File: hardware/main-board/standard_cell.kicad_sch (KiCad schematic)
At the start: 1 part

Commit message: stuff
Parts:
- added C1, C3, C5, C7: C, symbol Device:C
- added CH446Q1: ~, symbol SeniorDesign:CH446Q_Crossbar_Switch
- added D1, D3: 1N4148WT, Diode_SMD:D_SOD-523, symbol Diode:1N4148WT
- added Q1: PNP, symbol Simulation_SPICE:PNP
- added Q3: NPN, symbol Simulation_SPICE:NPN
- added U1: TL071, symbol Amplifier_Operational:TL071
- added U11, U3, U5, U7, U9: MCP4141-xxxx-P, Package_DIP:DIP-8_W7.62mm, symbol Potentiometer_Digital:MCP4141-xxxx-P
- renumbered CH446Q to CH446Q2
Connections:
- net Input: now also CH446Q2.33 (Y0), CH446Q1.33 (Y0)
- net C1_out: now reaches CH446Q2.1 (X14)
- net C1_out: now also C1.2
- net Output: now reaches CH446Q2.11 (Y7)
- net Output: now also CH446Q1.11 (Y7)
- net GND: now reaches CH446Q2.13 (Y6)
- net GND: now also CH446Q1.13 (Y6)
- net at CH446Q2.15 (Y5): now also CH446Q1.15 (Y5)
- net at CH446Q2.17 (Y4): now also CH446Q1.17 (Y4)
- net C2_in: now reaches CH446Q2.2 (x15)
- net C2_in: now also C3.1
- net C1_in: now reaches CH446Q2.24 (X13)
- net C1_in: now also C1.1
- net R5_out: now reaches CH446Q2.25 (X12)
- net R5_out: now also U5.6 (P0W), U5.7 (P0B)
- net R2_in: now reaches CH446Q2.26 (X5)
- net R2_in: now also U7.5 (P0A)
- net R1_out: now reaches CH446Q2.27 (X4)
- net R1_out: now also U11.6 (P0W), U11.7 (P0B)
- net R1_in: now reaches CH446Q2.28 (X3)
- net R1_in: now also U11.5 (P0A)
- net Op_neg: now reaches CH446Q2.29 (X2)
- net Op_neg: now also U1.2 (-)
- net R2_out: now reaches CH446Q2.3 (X6)
- net R2_out: now also U7.6 (P0W), U7.7 (P0B)
- net Op_pos: now reaches CH446Q2.30 (X1)
- net Op_pos: now also U1.3 (+)
- net Op_out: now reaches CH446Q2.31 (X0)
- net Op_out: now also U1.6
- net at CH446Q2.35 (Y1): now also CH446Q1.35 (Y1)
- net at CH446Q2.37 (Y2): now also CH446Q1.37 (Y2)
- net at CH446Q2.39 (Y3): now also CH446Q1.39 (Y3)
- net R3_in: now reaches CH446Q2.4 (X7)
- net R3_in: now also U9.5 (P0A)
- net R3_out: now reaches CH446Q2.5 (X8)
- net R3_out: now also U9.6 (P0W), U9.7 (P0B)
- net R4_in: now reaches CH446Q2.6 (X9)
- net R4_in: now also U3.5 (P0A)
- net R4_out: now reaches CH446Q2.7 (X10)
- net R4_out: now also U3.6 (P0W), U3.7 (P0B)
- net R5_in: now reaches CH446Q2.8 (X11)
- net R5_in: now also U5.5 (P0A)
- new net +5V: U1.7 (V+), U11.8 (V_{DD}), U3.8 (V_{DD}), U5.8 (V_{DD}), U7.8 (V_{DD}), U9.8 (V_{DD})
- new net -5V: U1.4 (V-), U11.4 (V_{SS}), U3.4 (V_{SS}), U5.4 (V_{SS}), U7.4 (V_{SS}), U9.4 (V_{SS})
- new net C2_out: C3.2, CH446Q1.31 (X0)
- new net C3_in: C5.1, CH446Q1.30 (X1)
- new net C3_out: C5.2, CH446Q1.29 (X2)
- new net C4_in: C7.1, CH446Q1.28 (X3)
- new net C4_out: C7.2, CH446Q1.27 (X4)
- new net D1_anode: CH446Q1.3 (X6), D1.2 (A)
- new net D1_cathode: CH446Q1.26 (X5), D1.1 (K)
- new net D2_anode: CH446Q1.5 (X8), D3.2 (A)
- new net D2_cathode: CH446Q1.4 (X7), D3.1 (K)
- new net NPN_Emitter: Q3.3 (E)
- new net NPN_base: CH446Q1.6 (X9), Q3.2 (B)
- new net NPN_collector: CH446Q1.8 (X11), Q3.1 (C)
- new net NPN_emitter: CH446Q1.7 (X10)
- new net PNP_base: CH446Q1.25 (X12), Q1.2 (B)
- new net PNP_collector: CH446Q1.1 (X14), Q1.1 (C)
- new net PNP_emitter: CH446Q1.24 (X13), Q1.3 (E)
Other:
- note added: "Digital Potentiometers (Pins x3-12)"
- note added: "OP-AMP Block (Pins x0-2)"
- moved on the sheet: CH446Q2A

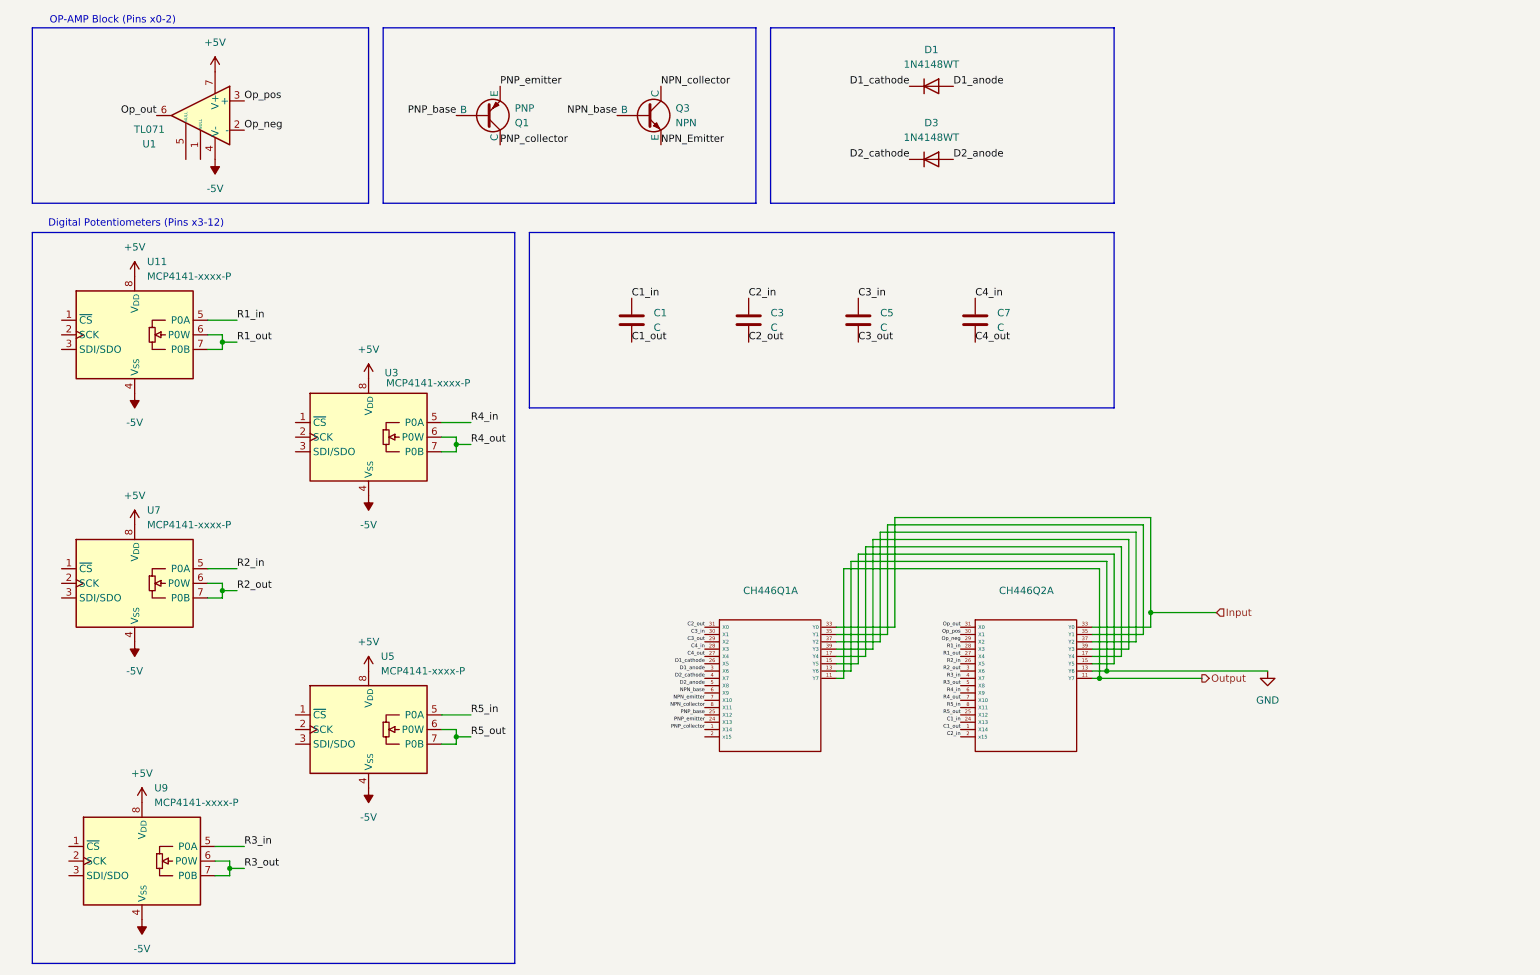
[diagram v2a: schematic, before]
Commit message: Changed cell design added new resistors
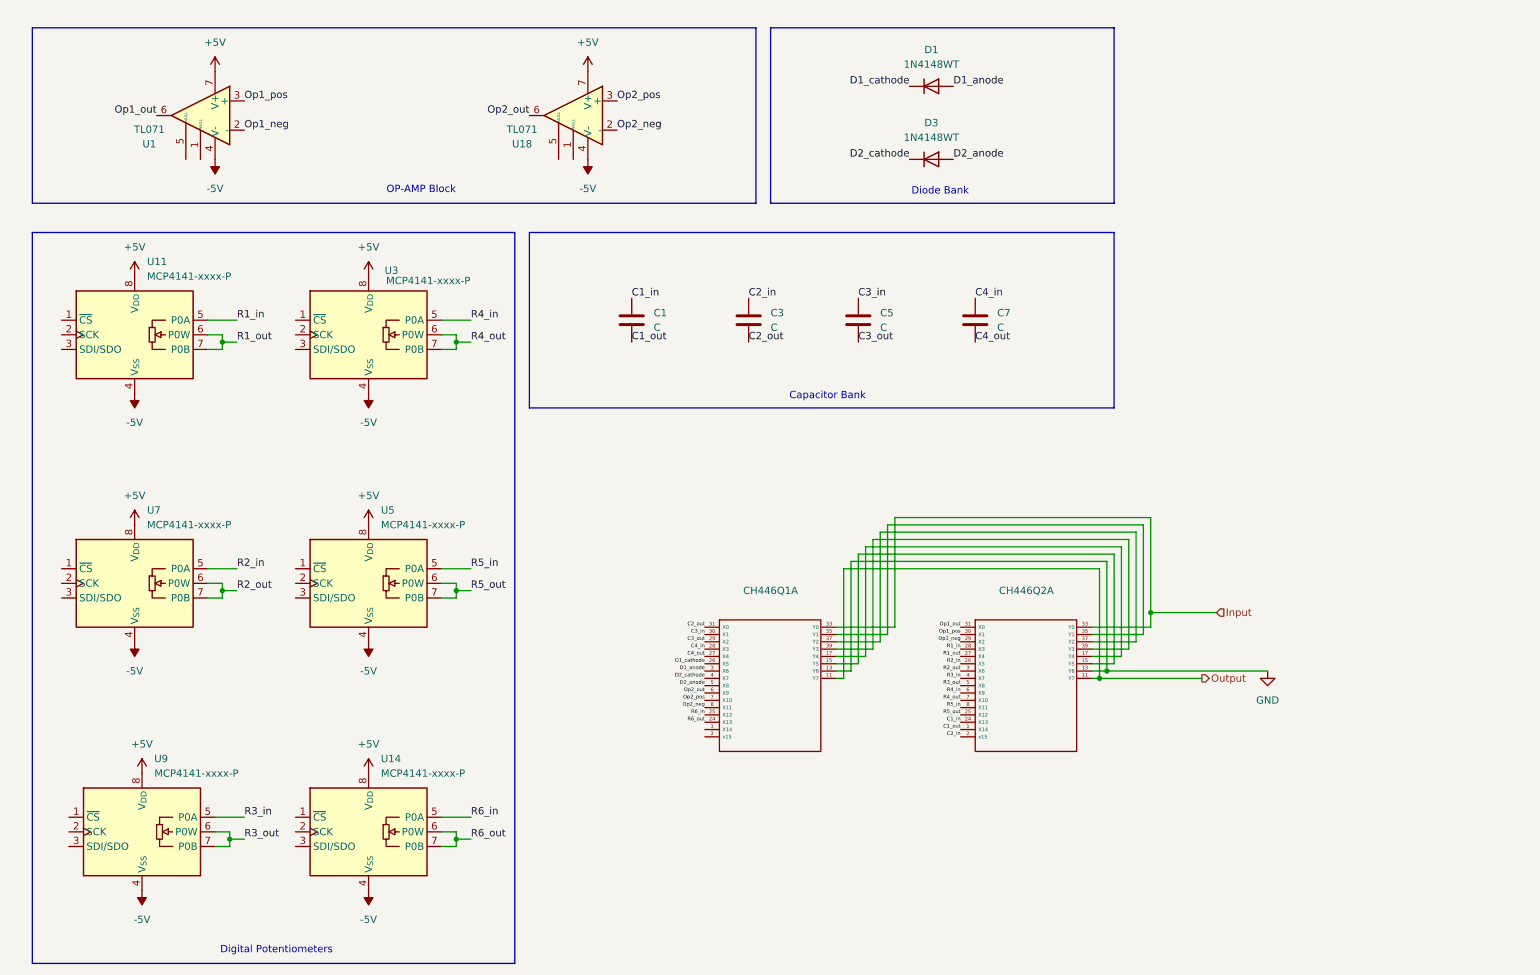
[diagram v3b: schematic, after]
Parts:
- removed Q1: PNP, symbol Simulation_SPICE:PNP
- removed Q3: NPN, symbol Simulation_SPICE:NPN
- added U14: MCP4141-xxxx-P, Package_DIP:DIP-8_W7.62mm, symbol Potentiometer_Digital:MCP4141-xxxx-P
- added U18: TL071, symbol Amplifier_Operational:TL071
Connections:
- net +5V: now also U14.8 (V_{DD}), U18.7 (V+)
- net -5V: now also U14.4 (V_{SS}), U18.4 (V-)
- net NPN_base renamed Op2_out
- net Op2_out: now also U18.6
- net NPN_collector renamed Op2_neg
- net Op2_neg: now also U18.2 (-)
- net NPN_emitter renamed Op2_pos
- net Op2_pos: now also U18.3 (+)
- net Op_neg renamed Op1_neg
- net Op_out renamed Op1_out
- net Op_pos renamed Op1_pos
- net PNP_base renamed R6_in
- net R6_in: now also U14.5 (P0A)
- net PNP_collector: no longer names the net of CH446Q1.1 (X14)
- net PNP_emitter renamed R6_out
- net R6_out: now also U14.6 (P0W), U14.7 (P0B)
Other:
- note added: "Capacitor Bank"
- note added: "Digital Potentiometers"
- note added: "Diode Bank"
- note added: "OP-AMP Block"
- note removed: "Digital Potentiometers (Pins x3-12)"
- note removed: "OP-AMP Block (Pins x0-2)"
- moved on the sheet: U3, U5, U9

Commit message: Clayton's fun routing fix
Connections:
- net Input_2: now reaches CH446Q1.35 (Y1), CH446Q2.35 (Y1)
- net Input_3: now reaches CH446Q1.37 (Y2), CH446Q2.37 (Y2)
- net Input renamed Input_1

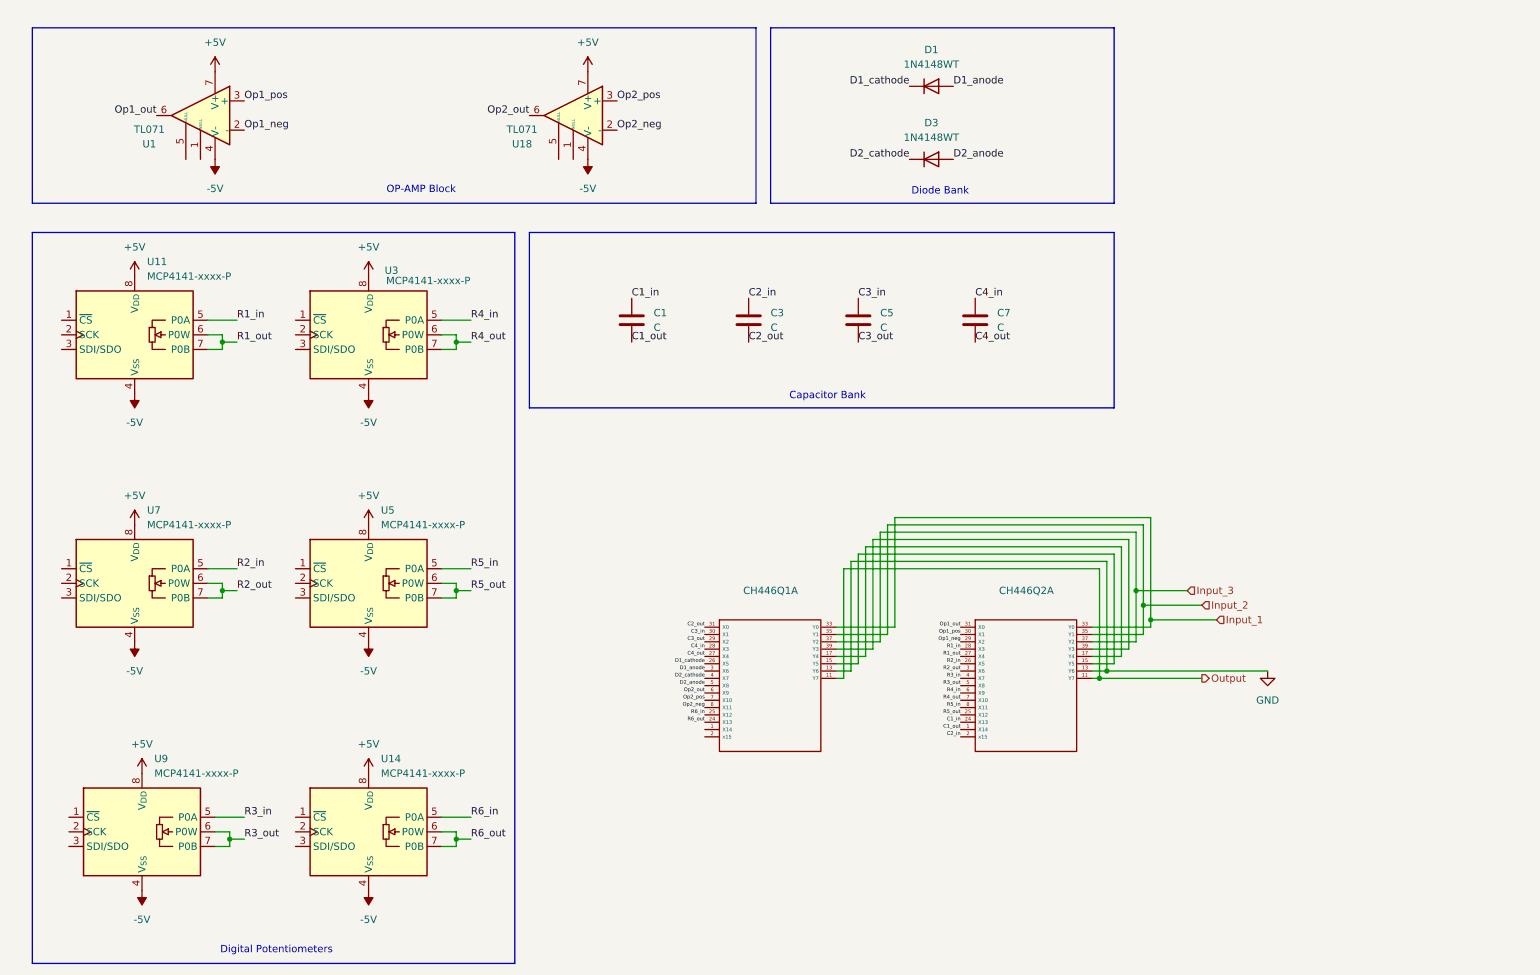
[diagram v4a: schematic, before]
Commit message: symbol update
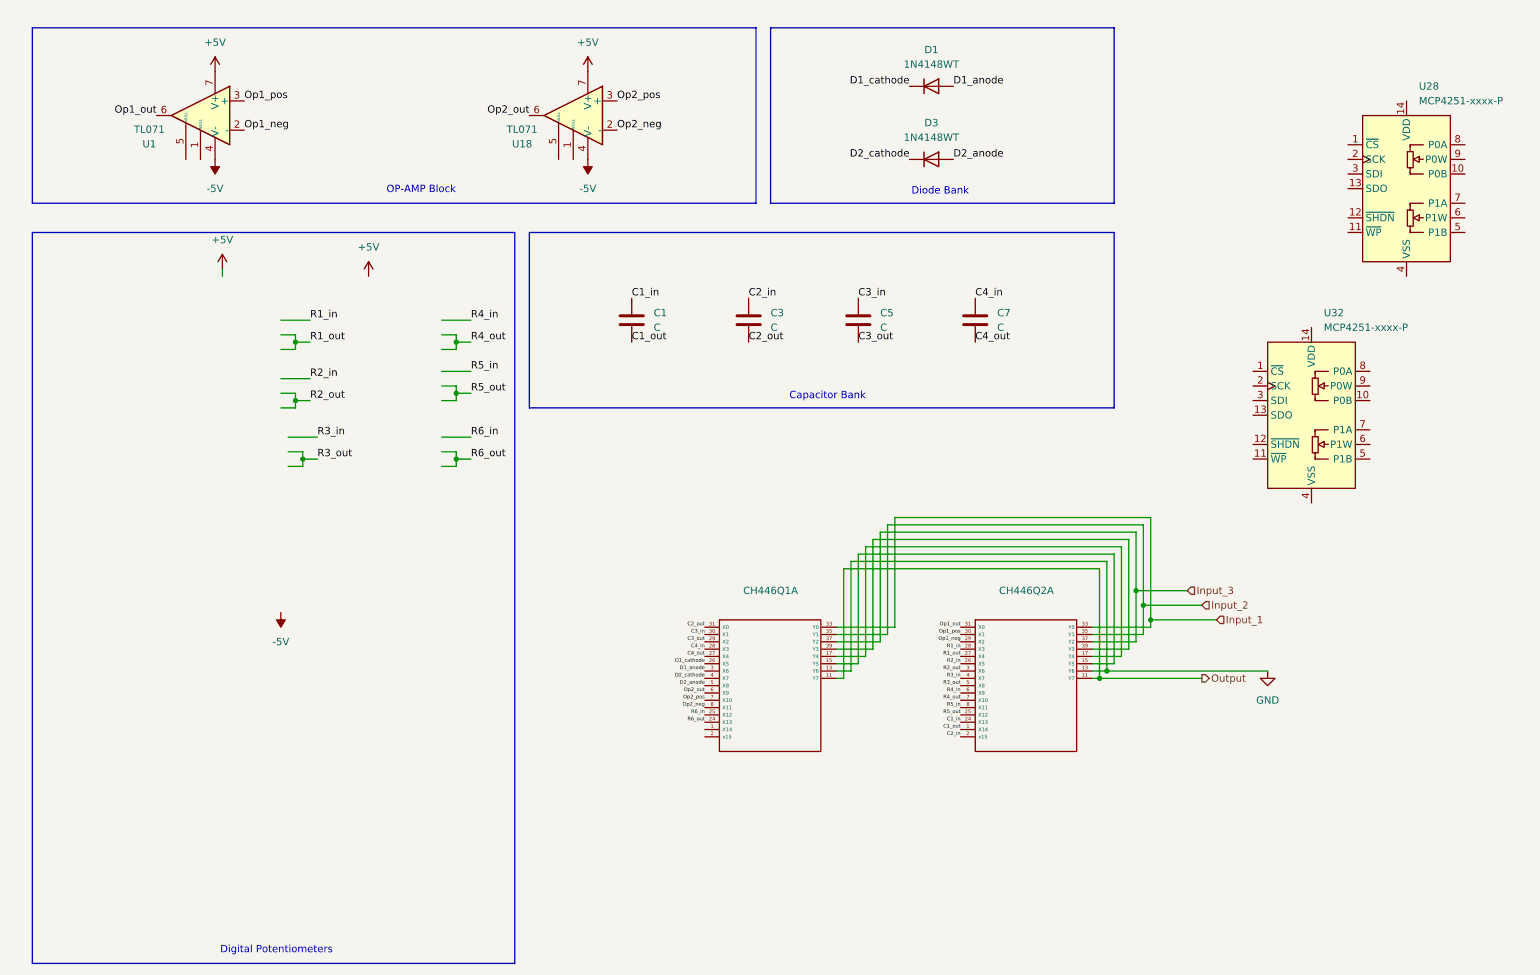
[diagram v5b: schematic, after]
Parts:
- removed U11, U14, U3, U5, U7, U9: MCP4141-xxxx-P, Package_DIP:DIP-8_W7.62mm, symbol Potentiometer_Digital:MCP4141-xxxx-P
- added U28, U32: MCP4251-xxxx-P, Package_DIP:DIP-14_W7.62mm, symbol Potentiometer_Digital:MCP4251-xxxx-P
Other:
- title: (none) -> Standard Cell Design Schematic

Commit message: Big Changes in the Schematic World
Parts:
- removed CH446Q1, CH446Q2: ~, symbol SeniorDesign:CH446Q_Crossbar_Switch
- removed U28, U32: MCP4251-xxxx-P, Package_DIP:DIP-14_W7.62mm, symbol Potentiometer_Digital:MCP4251-xxxx-P
- added U1: AD5263BRUZ200, AD5263BRUZ200:SOP65P640X120-24N, symbol SeniorDesign:AD5263BRUZ200
- added U2, U3: MT8816AF1, MT8816AF1:QFP80P1200X1200X120-44N, symbol SeniorDesign:MT8816AF1
- renumbered C3 to C2, C5 to C3, C7 to C4, D3 to D2, U1 to U4, U18 to U5
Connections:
- net C1_in: now also U3.24 (X13)
- net C1_out: now also U3.2 (X14)
- net C2_in: now also U3.3 (X15)
- net C2_out: now also U2.31 (X0)
- net C3_in: now also U2.30 (X1)
- net C3_out: now also U2.29 (X2)
- net C4_in: now also U2.28 (X3)
- net C4_out: now also U2.27 (X4)
- net D1_anode: now also U2.6 (X8)
- net D1_cathode: now also U2.5 (X7)
- net D2_anode: now also U2.8 (X10)
- net D2_cathode: now also U2.7 (X9)
- net GND: now also U2.10 (Y7), U3.10 (Y7)
- net Input_1: now also U2.37 (Y2), U3.37 (Y2)
- net Input_2: now also U2.35 (Y1), U3.35 (Y1)
- net Input_3: now also U2.32 (Y0), U3.32 (Y0)
- net Op1_neg: now also U3.29 (X2)
- net Op1_out: now also U3.31 (X0)
- net Op1_pos: now also U3.30 (X1)
- net Op2_neg: now also U2.24 (X13)
- net Op2_out: now also U2.9 (X11)
- net Op2_pos: now also U2.25 (X12)
- net Output: now also U2.13 (Y6), U3.13 (Y6)
- net R1_in: now also U1.1 (B1), U3.28 (X3)
- net R1_out: now also U1.2 (A1), U1.3 (W1), U3.27 (X4)
- net R2_in: now also U1.24 (B2), U3.26 (X5)
- net R2_out: now also U1.22 (W2), U1.23 (A2), U3.4 (X6)
- net R3_in: now also U1.4 (B3), U3.5 (X7)
- net R3_out: now also U1.5 (A3), U1.6 (W3), U3.6 (X8)
- net R4_in: now also U1.21 (B4), U3.7 (X9)
- net R4_out: now also U1.19 (W4), U1.20 (A4), U3.8 (X10)
- net R5_in: now also U2.1 (B1), U3.9 (X11)
- net R5_out: now also U2.2 (A1), U2.3 (W1), U3.25 (X12)
- net R6_in: now also U2.2 (X14), U2.24 (B2)
- net R6_out: now also U2.22 (W2), U2.23 (A2), U2.3 (X15)
- new net: U2.15 (Y5), U3.15 (Y5)
- new net: U2.17 (Y4), U3.17 (Y4)
- new net: U2.39 (Y3), U3.39 (Y3)

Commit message: fortnite info cache
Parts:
- added J5: Conn_01x02_Pin, symbol Connector:Conn_01x02_Pin
- C1: value C -> 1µF
- C2: value C -> 100nF
- C3: value C -> 10nF
- C4: value C -> 1nF
- renumbered U5 to U10, U2 to U11, U3 to U12, U4 to U7, U1 to U8, U2 to U9
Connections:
- net C1_in: now also U11.31 (X0); no longer U12.24 (X13)
- net C1_out: now also U11.30 (X1); no longer U12.2 (X14)
- net C2_in: now also U11.29 (X2); no longer U12.3 (X15)
- net C2_out: now also U11.28 (X3); no longer U11.31 (X0)
- net C3_in: now also U11.27 (X4); no longer U11.30 (X1)
- net C3_out: now also U11.26 (X5); no longer U11.29 (X2)
- net C4_in: now also U11.6 (X8); no longer U11.28 (X3)
- net C4_out: now also U11.7 (X9); no longer U11.27 (X4)
- net D1_anode: now also U11.5 (X7); no longer U11.6 (X8)
- net D1_cathode: now also U11.4 (X6); no longer U11.5 (X7)
- net D2_anode: now also U11.24 (X13); no longer U11.8 (X10)
- net D2_cathode: now also U11.25 (X12); no longer U11.7 (X9)
- net GND: now also U11.15 (Y5), U12.15 (Y5); no longer U11.10 (Y7), U12.10 (Y7)
- net Input_1: now also U11.32 (Y0), U12.32 (Y0); no longer U11.37 (Y2), U12.37 (Y2)
- net Input_3: now also U11.37 (Y2), U12.37 (Y2); no longer U11.32 (Y0), U12.32 (Y0)
- net Op2_neg: now also U12.26 (X5); no longer U11.24 (X13)
- net Op2_out: now also U12.28 (X3); no longer U11.9 (X11)
- net Op2_pos: now also U12.27 (X4); no longer U11.25 (X12)
- net Output: now also U11.39 (Y3), U12.39 (Y3); no longer U11.13 (Y6), U12.13 (Y6)
- net R1_in: now also U12.25 (X12); no longer U12.28 (X3)
- net R1_out: now also U12.24 (X13); no longer U12.27 (X4)
- net R2_in: now also U12.2 (X14); no longer U12.26 (X5)
- net R2_out: now also U12.3 (X15); no longer U12.4 (X6)
- net R3_in: now also U12.4 (X6); no longer U12.5 (X7)
- net R3_out: now also U12.5 (X7); no longer U12.6 (X8)
- net R4_in: now also U12.6 (X8); no longer U12.7 (X9)
- net R4_out: now also U12.7 (X9); no longer U12.8 (X10)
- net R5_in: now also U12.8 (X10); no longer U12.9 (X11)
- net R5_out: now also U12.9 (X11); no longer U12.25 (X12)
- net R6_in: now also U11.8 (X10); no longer U11.2 (X14)
- net R6_out: now also U11.9 (X11); no longer U11.3 (X15)
- new net: U11.10 (Y7), U12.10 (Y7)
- new net: U11.13 (Y6), U12.13 (Y6)
- new net J1_in: J5.1 (Pin_1), U11.2 (X14)
- new net J1_out: J5.2 (Pin_2), U11.3 (X15)
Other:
- note added: "User Component"
